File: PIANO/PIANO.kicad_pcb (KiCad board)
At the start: 2 copper layers, 46 parts, among them J1 640456-3, J1 Conn_01x02_Male, J2 USB_B_Micro, J3 Barrel_Jack_Switch, J4 22-23-2021, J5 640456-3, J6 640456-3, SW1 ON/OFF, SW2 RESET, U1 LF33_TO220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

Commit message: task: move components
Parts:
- moved J3 7.67 mm to (93.7, 109.0), turned to 90 degrees
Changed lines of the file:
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@@
   )
   (footprint "Connector_BarrelJack:BarrelJack_Horizontal" (layer "F.Cu")
-    (at 100.742 112.0725)
+    (at 93.726 108.966 90)
     (descr "DC Barrel Jack")
     (tags "Power Jack")
@@
     (property "Sheetname" "Switching Regulator")
     (attr through_hole)
-    (fp_text reference "J3" (at -9.895997 4.861) (layer "F.SilkS")
+    (fp_text reference "J3" (at -9.895997 4.861 90) (layer "F.SilkS")
       (effects (font (size 1 1) (thickness 0.15)))
     )
-    (fp_text value "Barrel_Jack_Switch" (at -6.2 -5.5) (layer "F.Fab")
+    (fp_text value "Barrel_Jack_Switch" (at -6.2 -5.5 90) (layer "F.Fab")
       (effects (font (size 1 1) (thickness 0.15)))
     )
-    (fp_text user "${REFERENCE}" (at -4.445997 -3.839) (layer "F.Fab")
+    (fp_text user "${REFERENCE}" (at -4.445997 -3.839 90) (layer "F.Fab")
       (effects (font (size 1 1) (thickness 0.15)))
     )
@@
     (fp_line (start -13.7 4.5) (end 0.8 4.5) (layer "F.Fab") (width 0.1))
     (fp_line (start 0.8 4.5) (end 0.8 -3.75) (layer "F.Fab") (width 0.1))
-    (pad "1" thru_hole rect (at 0 0) (size 3.5 3.5) (drill oval 1 3) (layers *.Cu *.Mask)
+    (pad "1" thru_hole rect (at 0 0 90) (size 3.5 3.5) (drill oval 1 3) (layers *.Cu *.Mask)
       (net 56 "Net-(D4-Pad1)") (pintype "passive"))
-    (pad "2" thru_hole roundrect (at -6 0) (size 3 3.5) (drill oval 1 3) (layers *.Cu *.Mask) (roundrect_rratio 0.25)
+    (pad "2" thru_hole roundrect (at -6 0 90) (size 3 3.5) (drill oval 1 3) (layers *.Cu *.Mask) (roundrect_rratio 0.25)
       (net 2 "GND") (pintype "passive"))
-    (pad "3" thru_hole roundrect (at -3 4.7) (size 3.5 3.5) (drill oval 3 1) (layers *.Cu *.Mask) (roundrect_rratio 0.25)
+    (pad "3" thru_hole roundrect (at -3 4.7 90) (size 3.5 3.5) (drill oval 3 1) (layers *.Cu *.Mask) (roundrect_rratio 0.25)
       (net 2 "GND") (pintype "passive"))
     (model "${KICAD6_3DMODEL_DIR}/Connector_BarrelJack.3dshapes/BarrelJack_Horizontal.wrl"

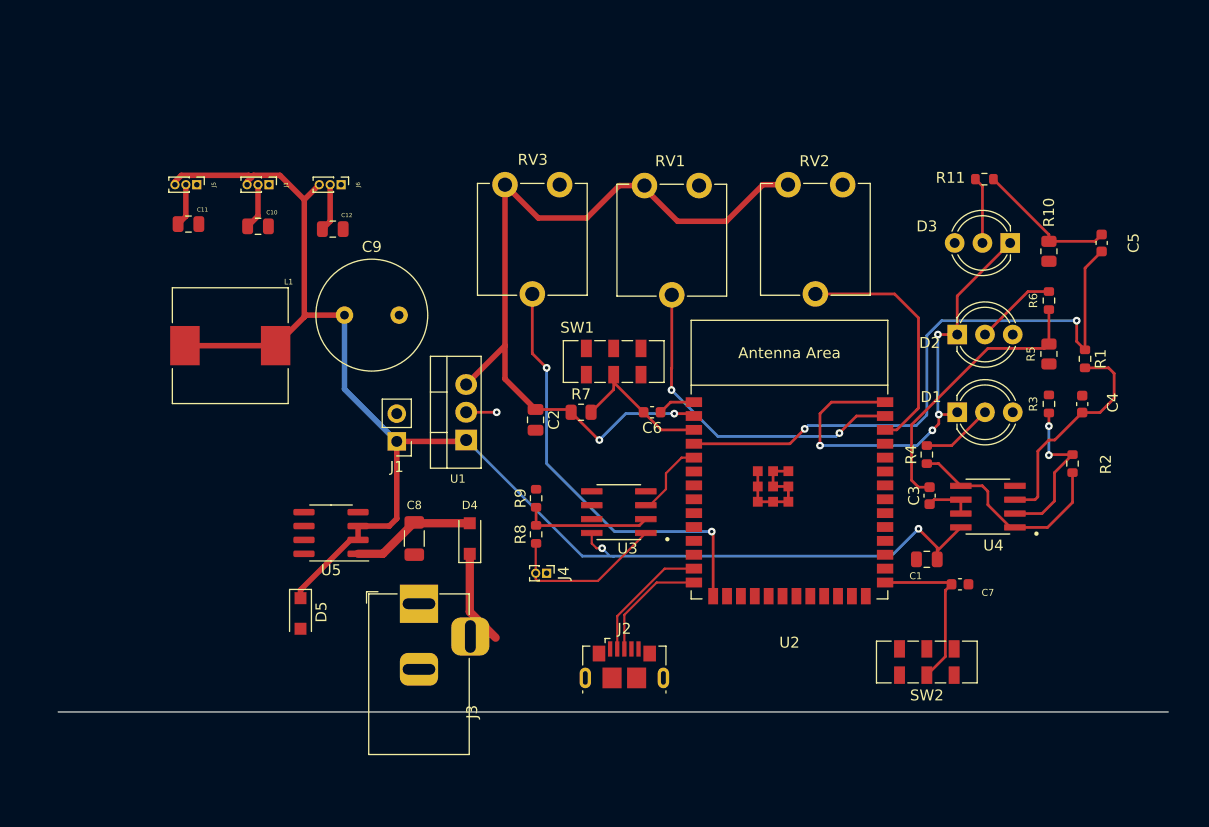
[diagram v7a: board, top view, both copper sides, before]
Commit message: Semi-Final Product
Pin headers added, traces cleaned up, and figured out some funky grounding issues.
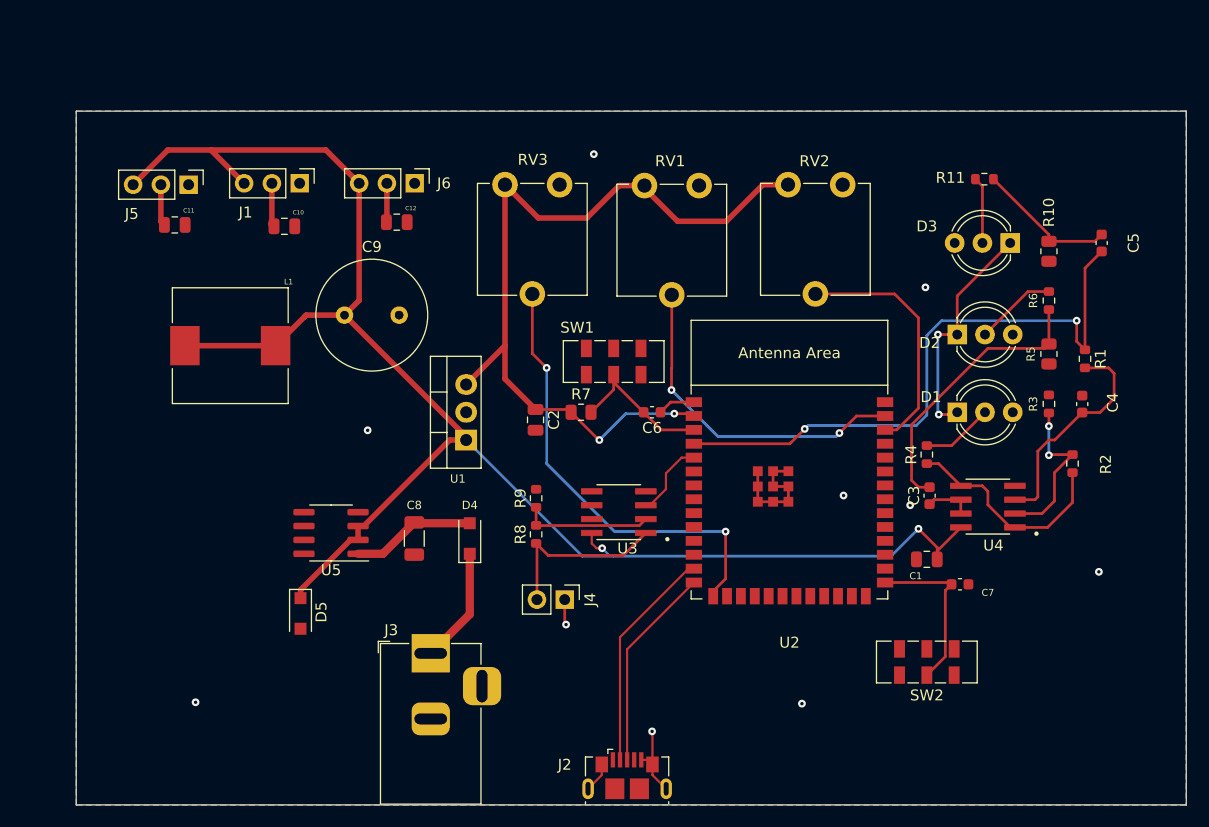
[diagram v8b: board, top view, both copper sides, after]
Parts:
- removed the J1 at (91.7, 94.1)
- J1, J5, J6: footprint Connector_PinHeader_1.00mm:PinHeader_1x03_P1.00mm_Vertical -> Connector_PinHeader_2.54mm:PinHeader_1x03_P2.54mm_Vertical
- J4: footprint Connector_PinHeader_1.00mm:PinHeader_1x02_P1.00mm_Vertical -> Connector_PinHeader_2.54mm:PinHeader_1x02_P2.54mm_Vertical
- moved J2 10.2 mm to (112.8, 124.7)
- moved J6 6.73 mm to (93.3, 70.5)
- moved C12 5.89 mm to (91.7, 74.0)
- moved J3 4.67 mm to (94.8, 113.5)
- moved J4 2.93 mm to (107.1, 108.6)
- moved J1 2.81 mm to (82.8, 70.5)
- moved C10 2.41 mm to (81.4, 74.4)
- moved C11 1.26 mm to (71.4, 74.3)
- moved J5 0.75 mm to (72.6, 70.6)
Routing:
- net GND: track 60.6 -> 48.0 mm, vias 5 -> 12
- net +5V: track 139.5 -> 151.2 mm
- net /D-: track 11.8 -> 20.6 mm
- net /D+: track 10.7 -> 18.8 mm
- net Net-(D4-Pad1): track 8.66 -> 10.6 mm
- net Net-(J4-Pad2): track 15.2 -> 16.5 mm
- net Net-(RV3-Pad2): track 39.7 -> 40.6 mm
- net /3 LED_STRIPS/Strip3: track 4.36 -> 3.58 mm
- added copper zone on B.Cu, net GND
- added copper zone on F.Cu, net GND
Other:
- board outline added: 101.6 x 63.5 mm
